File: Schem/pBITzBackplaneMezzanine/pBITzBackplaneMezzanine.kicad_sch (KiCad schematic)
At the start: 0 parts

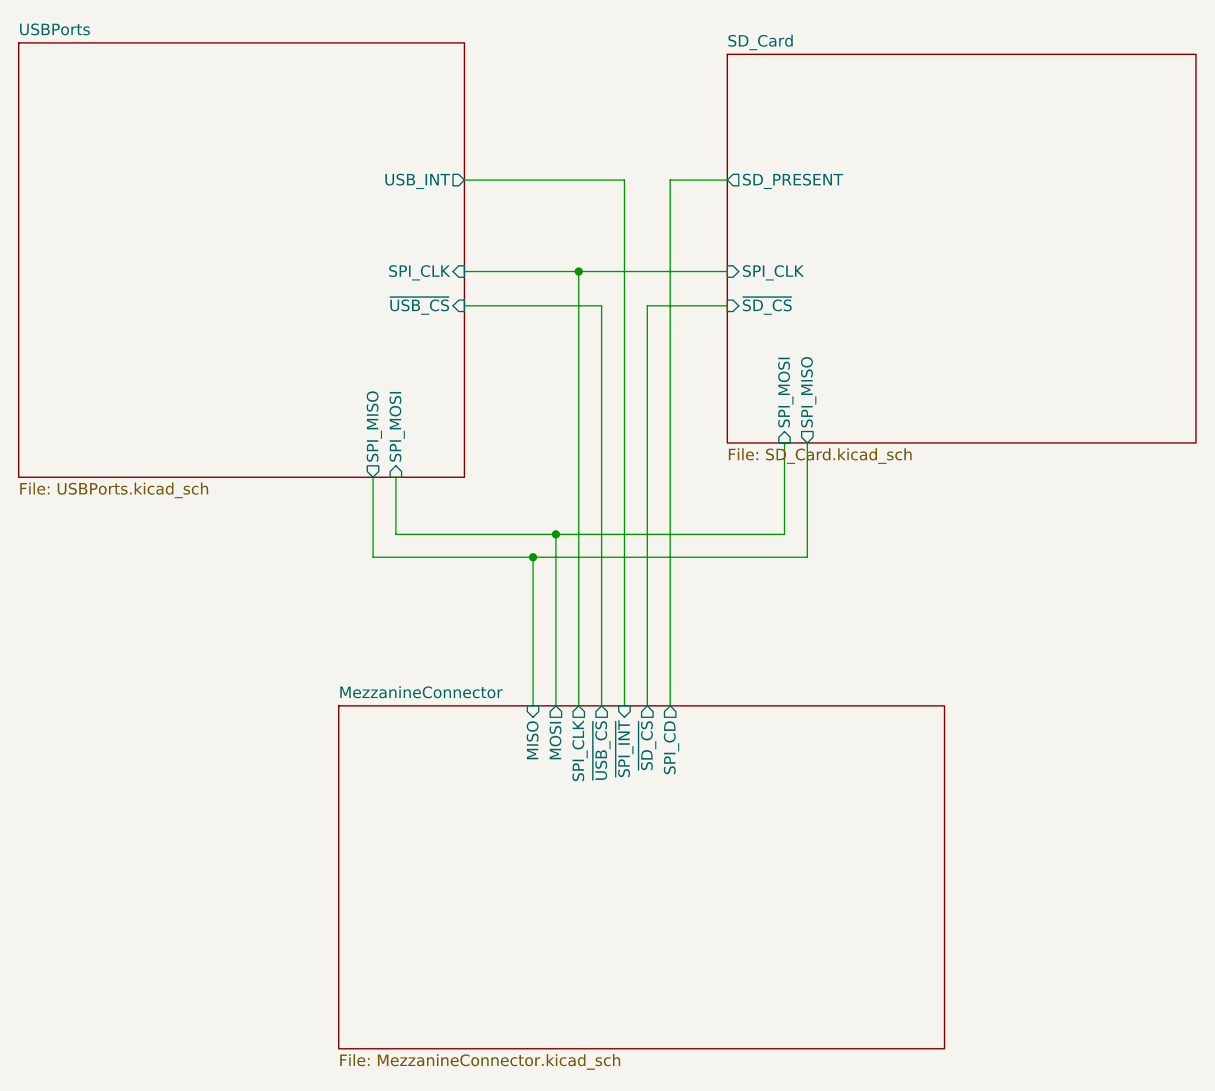
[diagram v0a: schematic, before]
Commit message: Major rework:
- Updated the Mezzanine to remove the slot connector and move it to the main board (facing the back)
-    The removal of the slot allowed for the removal of the FPC connector, which was a
     major source of complexity. The mezzanine now only has the SD card and USB connectors,
     which are much cheaper and easier to work with.
- The mezzanine is now more compact and cheaper to souirce

- The main board sees the addition of the external slot connector (coming from the mezzanine)
- Added power led on the mother board for easier debugging and testing
- Removed the free floating resistors to replace them with resistor packs
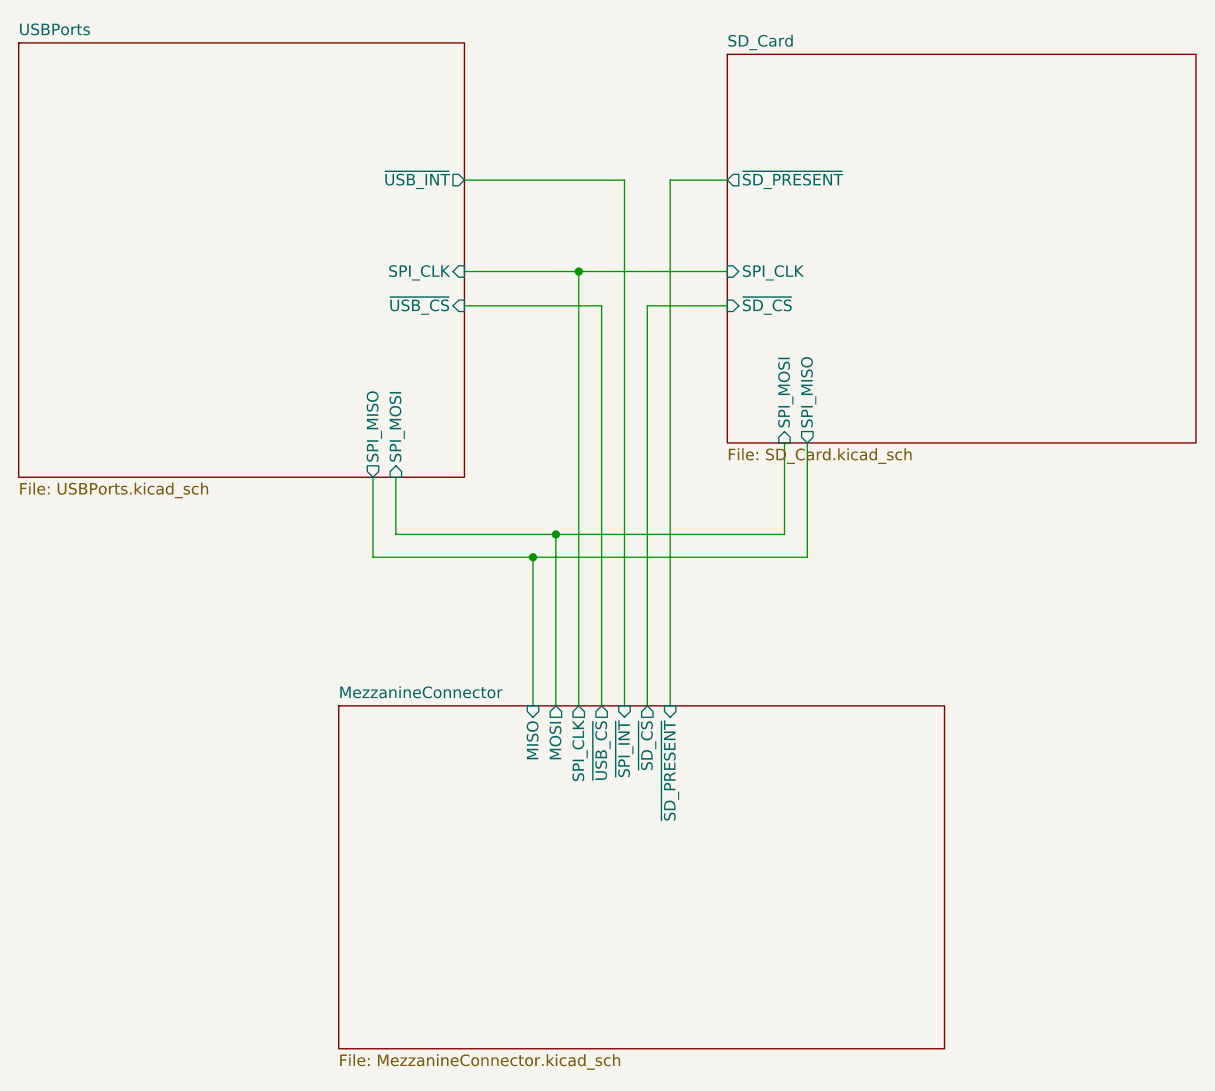
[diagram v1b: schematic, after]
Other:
- sheet MezzanineConnector ports: added ~{SD_PRESENT}; removed SPI_CD
- sheet SD_Card ports: added ~{SD_PRESENT}; removed SD_PRESENT
- sheet USBPorts ports: added ~{USB_INT}; removed USB_INT
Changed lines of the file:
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@@
 (kicad_sch
-	(version 20250114)
+	(version 20260306)
 	(generator "eeschema")
-	(generator_version "9.0")
+	(generator_version "10.0")
 	(paper "D")
 	(junction
@@
 		)
 		(fill
-			(color 0 0 0 0.0000)
+			(color 0 0 0 0)
 		)
 		(property "Sheetname" "USBPorts"
 			(at 80.01 48.8184 0)
+			(show_name no)
+			(do_not_autoplace no)
 			(effects
 				(font
@@
 		(property "Sheetfile" "USBPorts.kicad_sch"
 			(at 80.01 98.3746 0)
+			(show_name no)
+			(do_not_autoplace no)
 			(effects
 				(font
@@
 			)
 		)
-		(pin "USB_INT" output
-			(at 129.54 64.77 0)
-			(effects
-				(font
-					(size 1.27 1.27)
-				)
-				(justify right)
-			)
-		)
 		(pin "SPI_MISO" output
 			(at 119.38 97.79 270)
@@
 		(pin "~{USB_CS}" input
 			(at 129.54 78.74 0)
+			(effects
+				(font
+					(size 1.27 1.27)
+				)
+				(justify right)
+			)
+		)
+		(pin "~{USB_INT}" output
+			(at 129.54 64.77 0)
 			(effects
 				(font
@@
 		)
 		(fill
-			(color 0 0 0 0.0000)
+			(color 0 0 0 0)
 		)
 		(property "Sheetname" "MezzanineConnector"
 			(at 115.57 122.4784 0)
+			(show_name no)
+			(do_not_autoplace no)
 			(effects
 				(font
@@
 		(property "Sheetfile" "MezzanineConnector.kicad_sch"
 			(at 115.57 161.8746 0)
+			(show_name no)
+			(do_not_autoplace no)
 			(effects
 				(font
@@
 			)
 		)
-		(pin "SPI_CD" output
-			(at 152.4 123.19 90)
-			(effects
-				(font
-					(size 1.27 1.27)
-				)
-				(justify right)
-			)
-		)
 		(pin "~{USB_CS}" output
 			(at 144.78 123.19 90)
@@
 		(pin "SPI_CLK" output
 			(at 142.24 123.19 90)
+			(effects
+				(font
+					(size 1.27 1.27)
+				)
+				(justify right)
+			)
+		)
+		(pin "~{SD_PRESENT}" input
+			(at 152.4 123.19 90)
 			(effects
 				(font
@@
 		)
 		(fill
-			(color 0 0 0 0.0000)
+			(color 0 0 0 0)
 		)
 		(property "Sheetname" "SD_Card"
 			(at 158.75 50.0884 0)
+			(show_name no)
+			(do_not_autoplace no)
 			(effects
 				(font
@@
 		(property "Sheetfile" "SD_Card.kicad_sch"
 			(at 158.75 94.5646 0)
+			(show_name no)
+			(do_not_autoplace no)
 			(effects
 				(font
@@
 			)
 		)
-		(pin "SD_PRESENT" output
-			(at 158.75 64.77 180)
-			(effects
-				(font
-					(size 1.27 1.27)
-				)
-				(justify left)
-			)
-		)
 		(pin "SPI_MOSI" input
 			(at 165.1 93.98 270)
@@
 			(effects
 				(font
+					(size 1.27 1.27)
+				)
+				(justify left)
+			)
+		)
+		(pin "~{SD_PRESENT}" output
+			(at 158.75 64.77 180)
+			(effects
+				(font

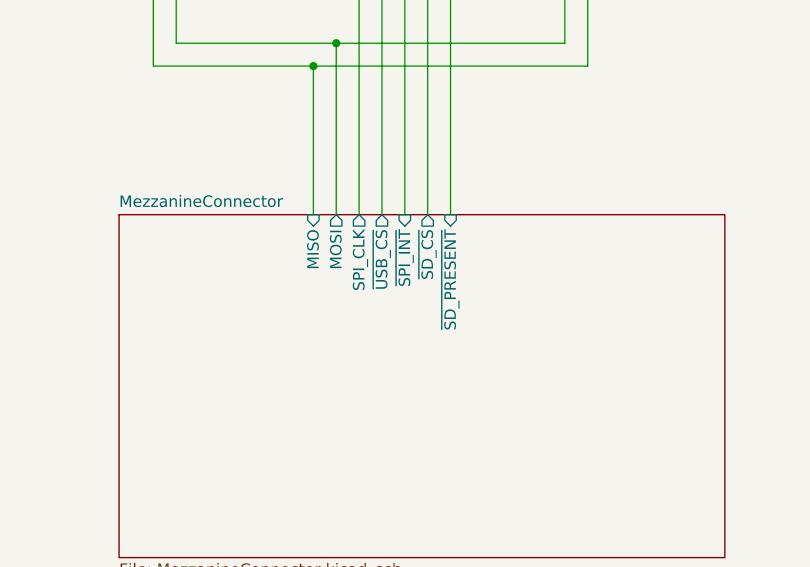
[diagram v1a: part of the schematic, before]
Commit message: Removed the rotary switch selector
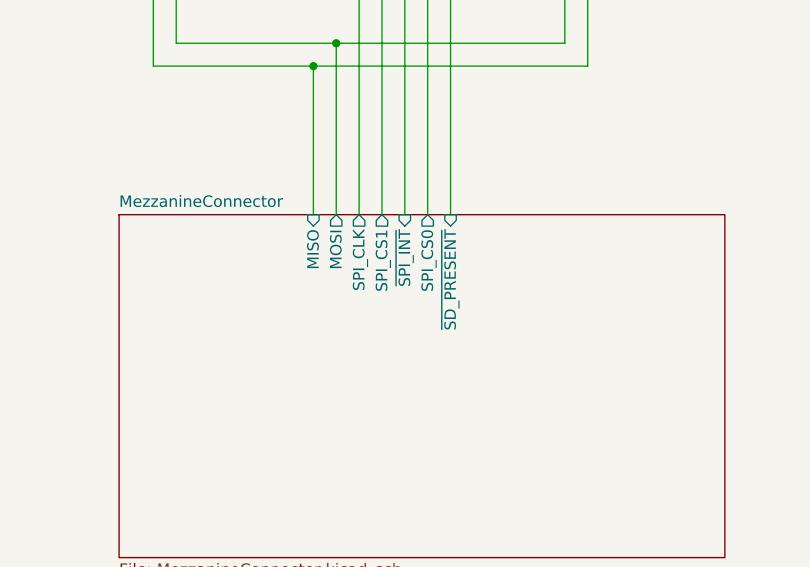
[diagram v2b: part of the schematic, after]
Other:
- sheet MezzanineConnector ports: added SPI_CS0, SPI_CS1; removed ~{SD_CS}, ~{USB_CS}
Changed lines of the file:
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@@
-			)
-		)
-		(pin "~{USB_CS}" output
-			(at 144.78 123.19 90)
-			(effects
-				(font
-					(size 1.27 1.27)
-				)
-				(justify right)
-			)
-		)
-		(pin "~{SD_CS}" output
-			(at 149.86 123.19 90)
-			(effects
-				(font
-					(size 1.27 1.27)
-				)
-				(justify right)
 			)
 		)
@@
 			(effects
 				(font
+					(size 1.27 1.27)
+				)
+				(justify right)
+			)
+		)
+		(pin "SPI_CS0" output
+			(at 149.86 123.19 90)
+			(effects
+				(font
+					(size 1.27 1.27)
+				)
+				(justify right)
+			)
+		)
+		(pin "SPI_CS1" output
+			(at 144.78 123.19 90)
+			(effects
+				(font
